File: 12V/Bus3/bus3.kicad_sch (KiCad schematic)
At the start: 3 parts, among them J1 Conn_01x10_Pin

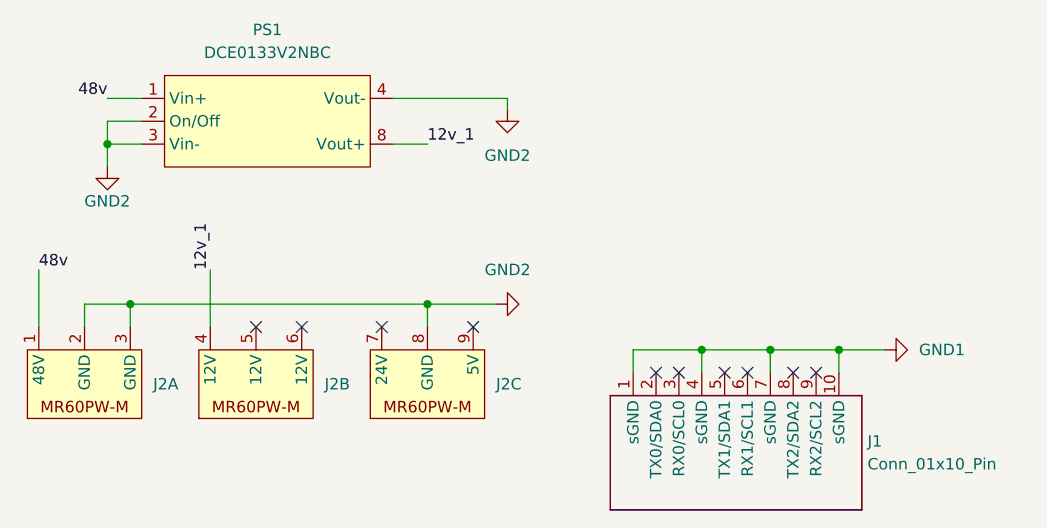
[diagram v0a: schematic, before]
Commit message: Complete 12V
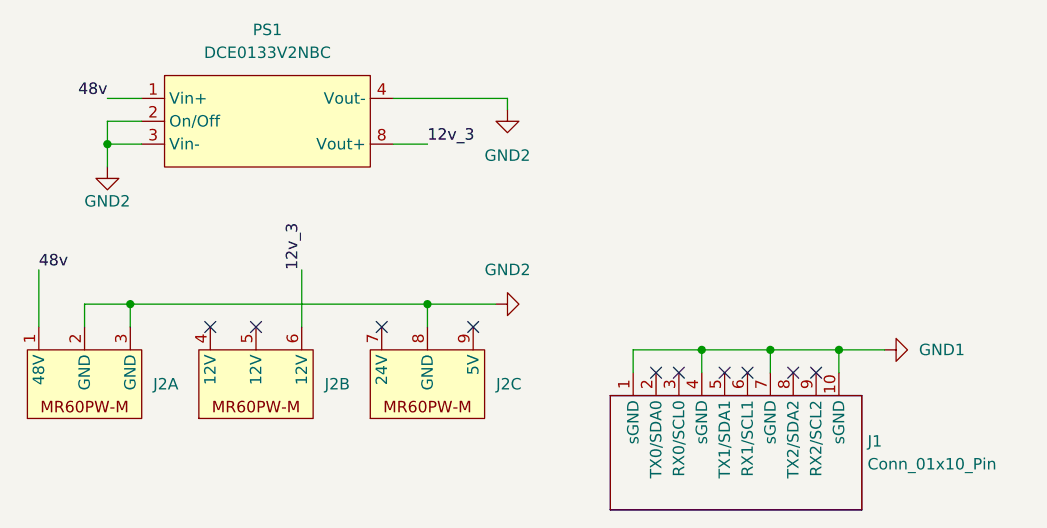
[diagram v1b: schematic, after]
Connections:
- net 12v_3: now reaches J2.6 (12V)
- net 12v_3: now also PS1.8 (Vout+)
- net 12v_1: no longer names the net of J2.4 (12V)
- net 12v_1: no longer PS1.8 (Vout+)
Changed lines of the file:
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@@
   (no_connect (at 161.29 121.92))
   (no_connect (at 151.13 121.92))
+  (no_connect (at 137.16 121.92))
   (no_connect (at 199.39 127))
   (no_connect (at 181.61 127))
@@
   (no_connect (at 191.77 127))
   (no_connect (at 189.23 127))
-  (no_connect (at 142.24 121.92))
+  (no_connect (at 132.08 121.92))
   (no_connect (at 196.85 127))
-  (no_connect (at 137.16 121.92))
   (wire (pts (xy 165.1 96.52) (xy 165.1 97.79))
     (stroke (width 0) (type default))
@@
     (stroke (width 0) (type default))
   )
-  (wire (pts (xy 132.08 115.57) (xy 132.08 121.92))
-    (stroke (width 0) (type default))
-  )
   (wire (pts (xy 201.93 124.46) (xy 207.01 124.46))
     (stroke (width 0) (type default))
@@
     (stroke (width 0) (type default))
   )
+  (wire (pts (xy 142.24 115.57) (xy 142.24 121.92))
+    (stroke (width 0) (type default))
+  )
   (wire (pts (xy 120.65 101.6) (xy 120.65 104.14))
     (stroke (width 0) (type default))
@@
     (stroke (width 0) (type default))
     (fill (type none))
-  )
-  (label "12v_1" (at 132.08 115.57 90) (fields_autoplaced)
-    (effects (font (size 1.27 1.27)) (justify left bottom))
   )
   (label "48v" (at 120.65 96.52 180) (fields_autoplaced)
     (effects (font (size 1.27 1.27)) (justify right bottom))
   )
-  (label "12v_1" (at 156.21 101.6 0) (fields_autoplaced)
+  (label "12v_3" (at 156.21 101.6 0) (fields_autoplaced)
+    (effects (font (size 1.27 1.27)) (justify left bottom))
+  )
+  (label "12v_3" (at 142.24 115.57 90) (fields_autoplaced)
     (effects (font (size 1.27 1.27)) (justify left bottom))
   )
@@
     (pin "8")
     (instances
-      (project "bus1"
+      (project "bus3"
         (path "/447f7668-e44a-4076-b3cb-4e0f6120b53c"
           (reference "PS1") (unit 1)
@@
     (pin "1")
     (instances
-      (project "bus1"
+      (project "bus3"
         (path "/447f7668-e44a-4076-b3cb-4e0f6120b53c"
           (reference "#PWR07") (unit 1)
@@
     (pin "9")
     (instances
-      (project "bus1"
+      (project "bus3"
         (path "/447f7668-e44a-4076-b3cb-4e0f6120b53c"
           (reference "J2") (unit 1)
@@
     (pin "9")
     (instances
-      (project "bus1"
+      (project "bus3"
         (path "/447f7668-e44a-4076-b3cb-4e0f6120b53c"
           (reference "J2") (unit 2)
@@
     (pin "9")
     (instances
-      (project "bus1"
+      (project "bus3"
         (path "/447f7668-e44a-4076-b3cb-4e0f6120b53c"
           (reference "J1") (unit 1)
@@
     (pin "9")
     (instances
-      (project "bus1"
+      (project "bus3"
         (path "/447f7668-e44a-4076-b3cb-4e0f6120b53c"
           (reference "J2") (unit 3)
@@
     (pin "1")
     (instances
-      (project "bus1"
+      (project "bus3"
         (path "/447f7668-e44a-4076-b3cb-4e0f6120b53c"
           (reference "#PWR06") (unit 1)
@@
     (pin "1")
     (instances
-      (project "bus1"
+      (project "bus3"
         (path "/447f7668-e44a-4076-b3cb-4e0f6120b53c"
           (reference "#PWR01") (unit 1)
@@
     (pin "1")
     (instances
-      (project "bus1"
+      (project "bus3"
         (path "/447f7668-e44a-4076-b3cb-4e0f6120b53c"
           (reference "#PWR02") (unit 1)
